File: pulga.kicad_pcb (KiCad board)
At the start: 2 copper layers, 38 x 34.1 mm, 20 parts, among them U2 ESP32-C3-WROOM-02, U3 TCAN332G

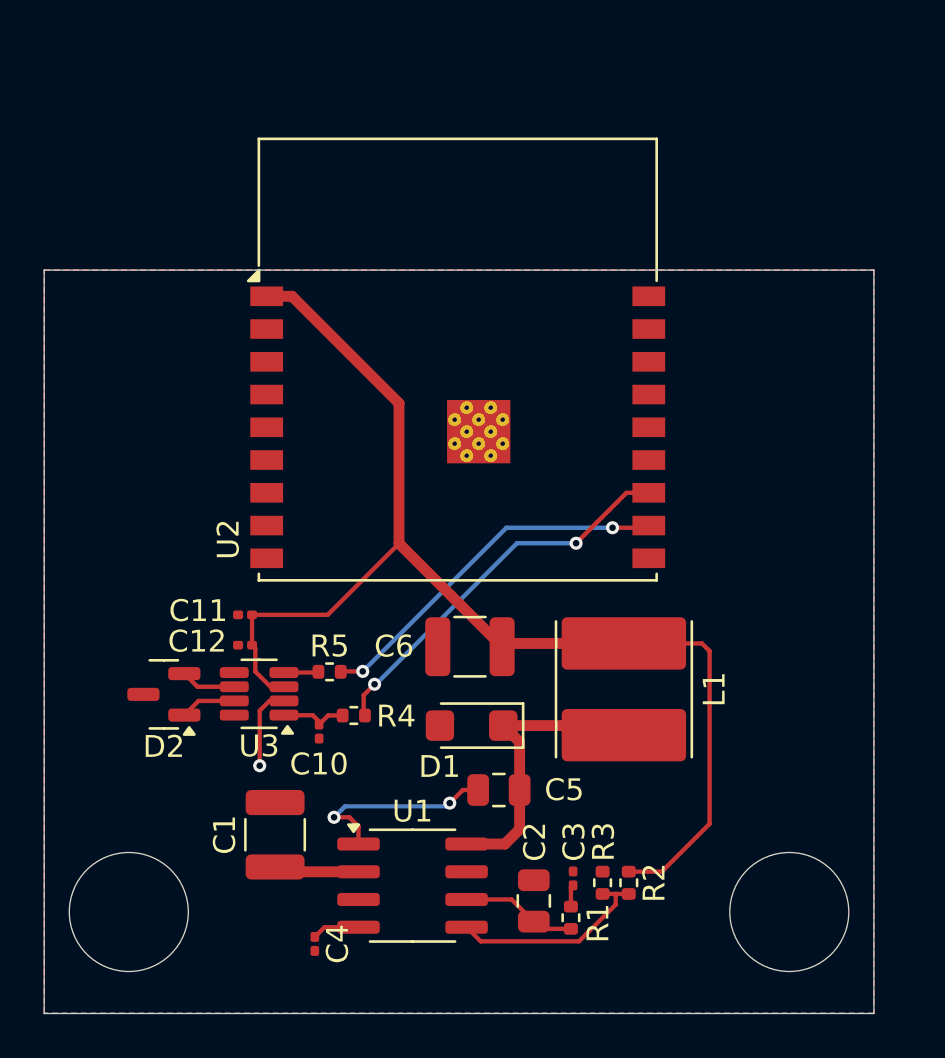
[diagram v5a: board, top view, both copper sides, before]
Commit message: adicionando sistema de controle para o modo de boot do esp32
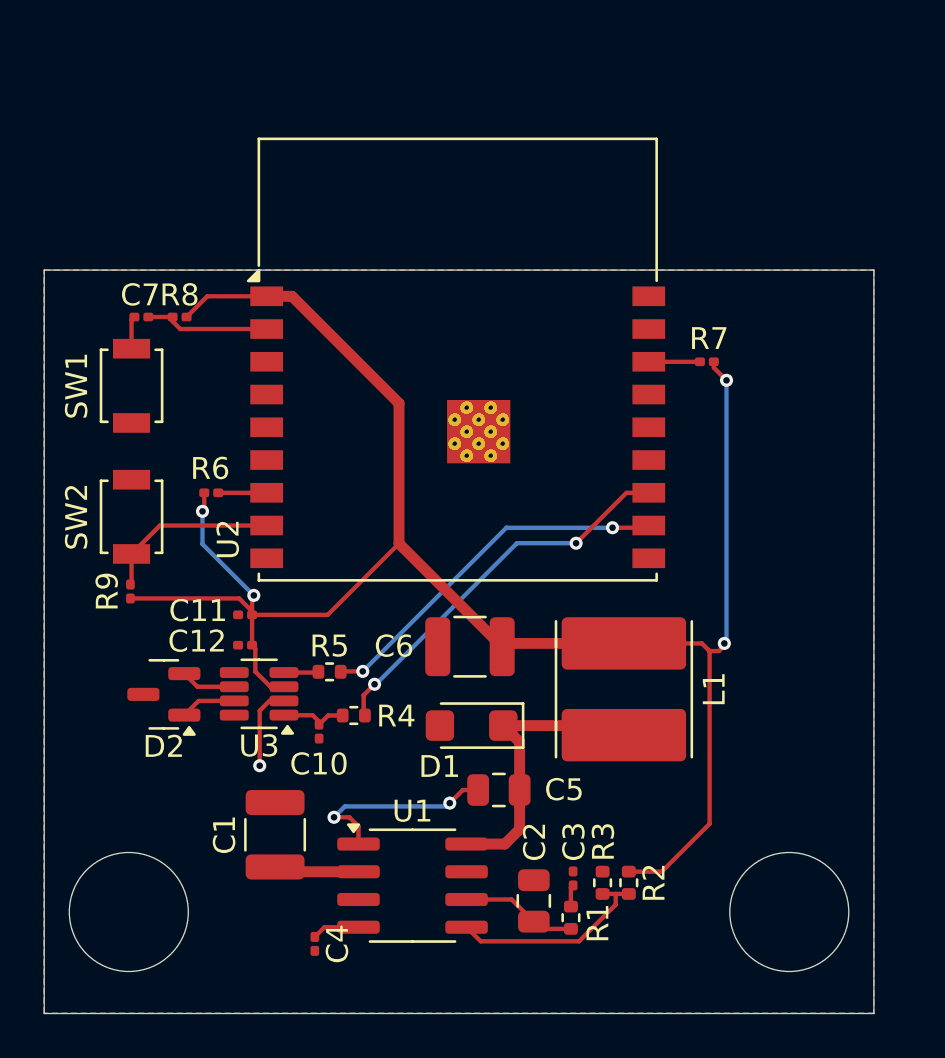
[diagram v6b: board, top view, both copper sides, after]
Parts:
- added C7: 100n, Capacitor_SMD:C_0201_0603Metric, F.Cu at (97.0, 48.0)
- added R6: 10k, Resistor_SMD:R_0201_0603Metric, F.Cu at (100.2, 56.0)
- added R7: 10k, Resistor_SMD:R_0201_0603Metric, F.Cu at (123.0, 50.0)
- added R8: 10k, Resistor_SMD:R_0201_0603Metric, F.Cu at (98.8, 48.0)
- added R9: 10k, Resistor_SMD:R_0201_0603Metric, F.Cu at (96.5, 60.6)
- added SW1: SW_Push, Button_Switch_SMD:SW_SPST_B3U-1000P, F.Cu at (96.6, 51.1)
- added SW2: SW_Push, Button_Switch_SMD:SW_SPST_B3U-1000P, F.Cu at (96.6, 57.1)
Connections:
- U2 pad 16: unconnected-(U2-IO2-Pad16) -> Net-(U2-IO2)
- U2 pad 2: unconnected-(U2-EN-Pad2) -> chip_en
- U2 pad 7: unconnected-(U2-IO8-Pad7) -> Net-(U2-IO8)
- U2 pad 8: unconnected-(U2-IO9-Pad8) -> boot
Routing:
- net 3V3: track 56.0 -> 86.7 mm, vias 0 -> 4
- net boot: track 0.00 -> 8.15 mm
- net chip_en: track 0.00 -> 5.76 mm
- net Net-(U2-IO2): track 0.00 -> 2.34 mm
- net Net-(U2-IO8): track 0.00 -> 2.22 mm
- net Net-(C7-Pad2): track 0.00 -> 1.50 mm

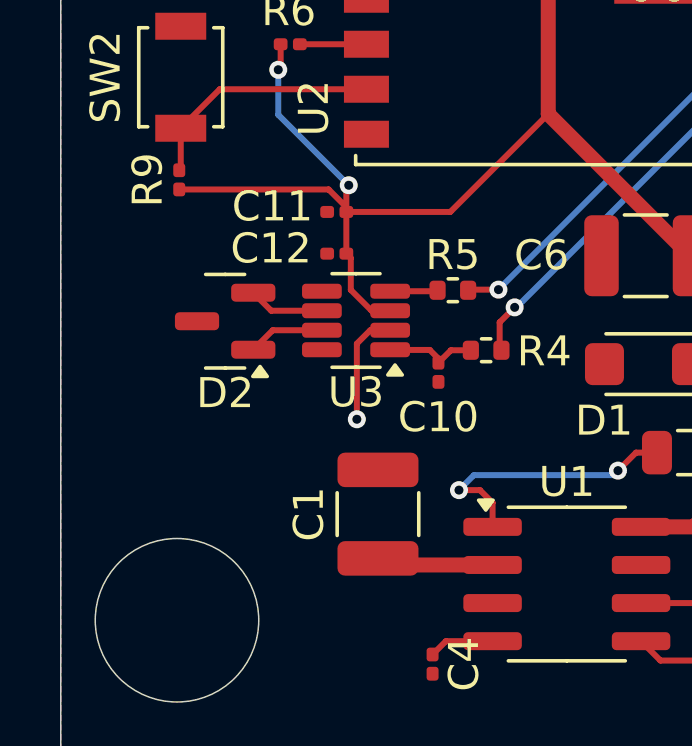
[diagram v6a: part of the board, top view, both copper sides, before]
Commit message: adicionando o esquemático e footprint dos 4 pinos principais (12v, gnd, can_h e can_l) que vem do OBD
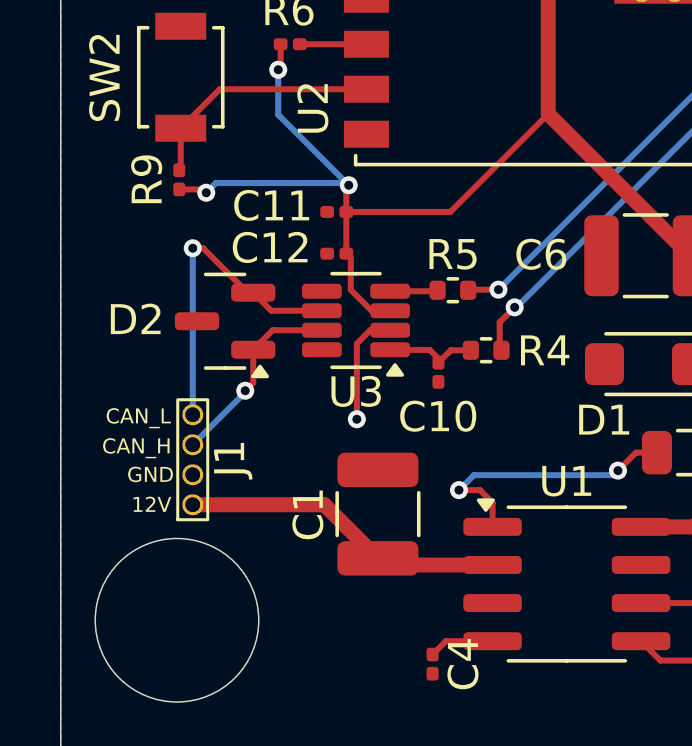
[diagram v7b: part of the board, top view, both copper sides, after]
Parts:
- added J1: Conn_01x04_Pin, through_hole:obd_main_pins, F.Cu at (99.5, 69.9)
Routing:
- net can_l: track 2.54 -> 10.7 mm, vias 0 -> 1
- net 12V: track 3.91 -> 10.8 mm
- net can_h: track 2.56 -> 6.56 mm, vias 0 -> 1
- net 3V3: track 86.7 -> 86.8 mm, vias 4 -> 5

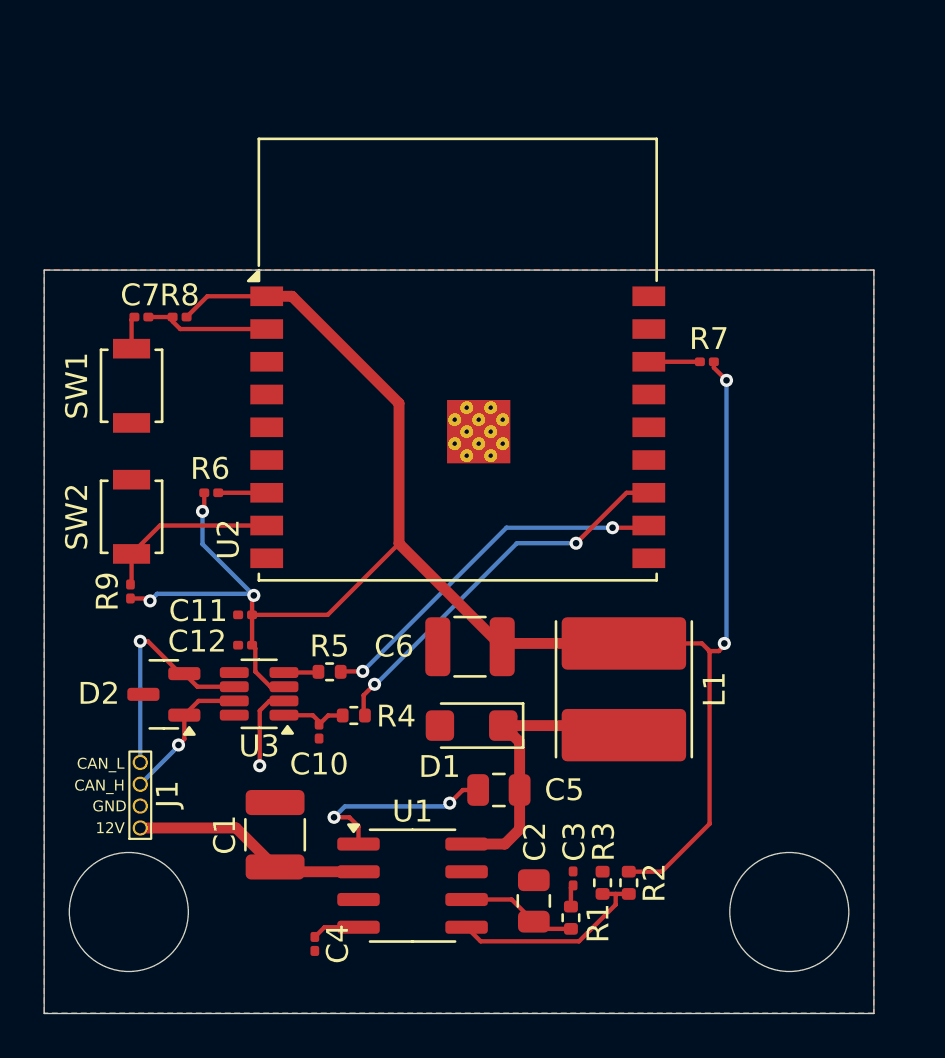
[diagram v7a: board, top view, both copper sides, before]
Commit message: ajeitando os pinos de conexão do OBD
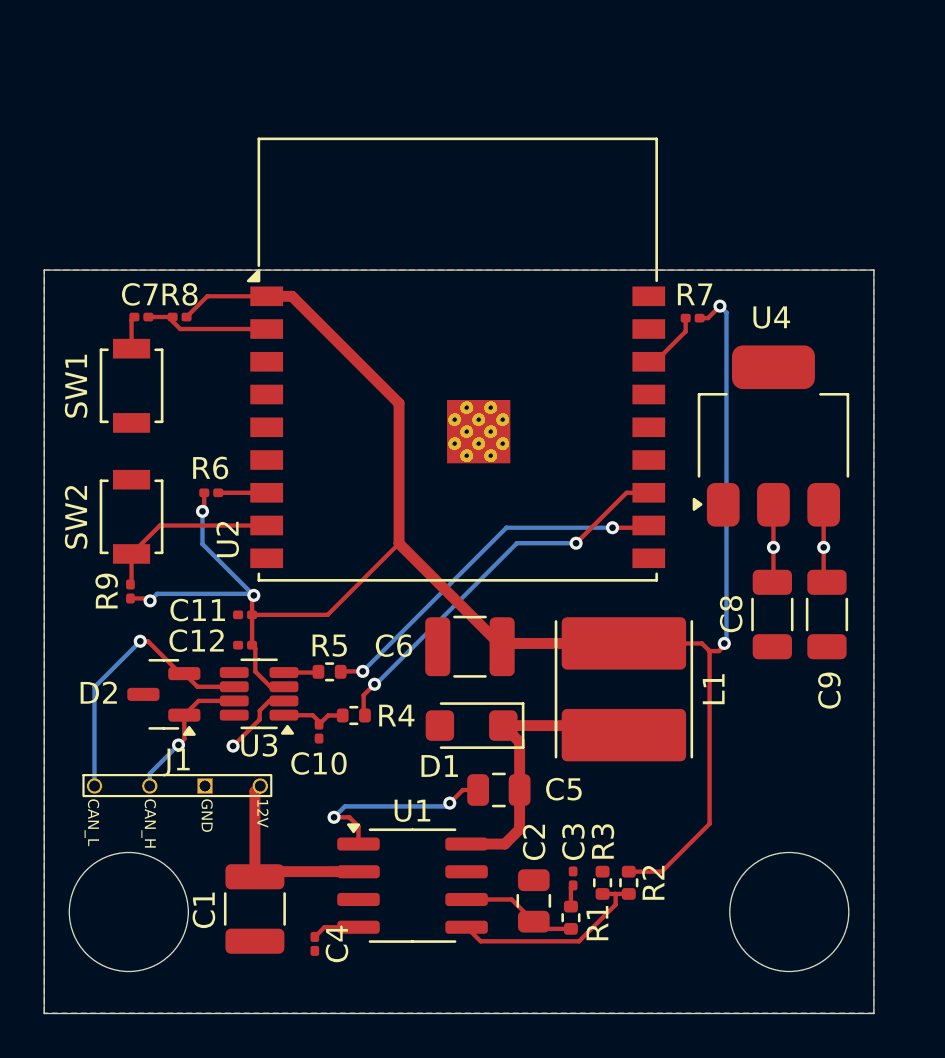
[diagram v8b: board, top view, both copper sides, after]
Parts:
- added C8: 22u, Capacitor_SMD:C_1206_3216Metric, F.Cu at (126.0, 61.6)
- added C9: 10u, Capacitor_SMD:C_1206_3216Metric, F.Cu at (128.4, 61.6)
- added U4: AMS1117-3.3, Package_TO_SOT_SMD:SOT-223-3_TabPin2, F.Cu at (126.0, 53.5)
- moved C1 3.52 mm to (102.2, 75.1), turned to -90 degrees
- moved J1 2.17 mm to (98.7, 71.9), turned to 0 degrees
- moved R7 2.10 mm to (122.3, 48.0)
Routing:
- net 3V3: track 86.8 -> 93.9 mm, vias 5 -> 6
- net 5V: track 0.00 -> 3.61 mm, vias 0 -> 1
- net can_l: track 10.7 -> 12.7 mm
- net 12V: track 10.8 -> 9.10 mm
- net Net-(U2-IO2): track 2.34 -> 2.88 mm
